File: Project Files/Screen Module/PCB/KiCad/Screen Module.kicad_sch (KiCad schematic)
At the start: 17 parts, among them J1 Conn_01x19_Male, J2 Conn_01x19_Male, J3 Conn_02x04_Top_Bottom, J4 Conn_02x03_Top_Bottom, Q1 BC817, SW1 SW_Push, SW2 SW_Push

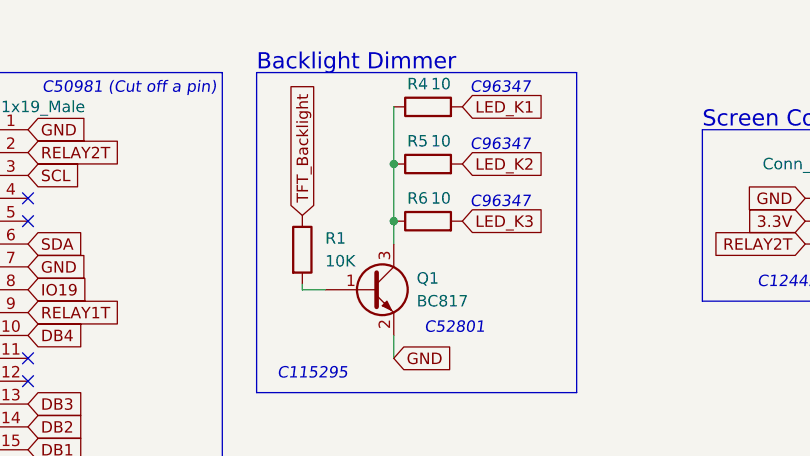
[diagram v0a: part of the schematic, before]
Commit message: Updated PCB to fix several issues Wall Module: Fixed relay flyback diodes pointing in the wrong direction.
Screen PCB:
Fixed display LED resistors to be a more suitable value.
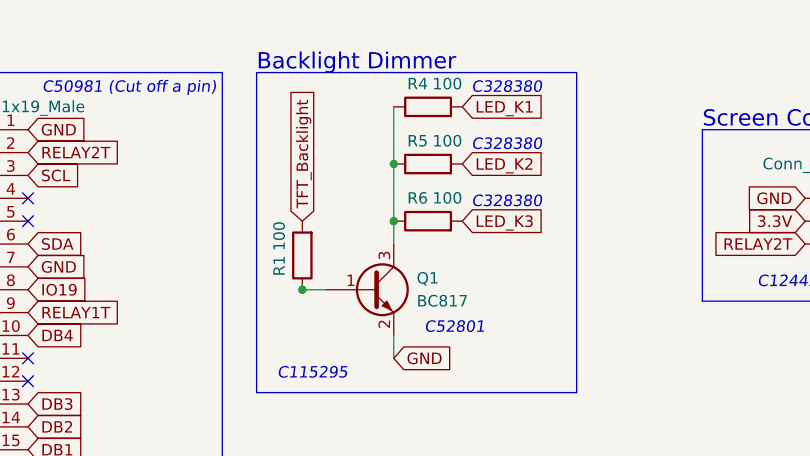
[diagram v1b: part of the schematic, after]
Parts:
- R1: value 10K -> 100
- R4, R5, R6: value 10 -> 100
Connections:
- net TFT_Backlight: now also R1.2; no longer R1.1
- net at Q1.1 (B): now also R1.1; no longer R1.2
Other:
- note added: "C328380"
- note removed: "C96347"
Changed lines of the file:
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@@
 (kicad_sch (version 20211123) (generator eeschema)
   (paper "A4")
+  (junction (at 87.63 45.72) (diameter 0) (color 0 0 0 0)
+  )
   (junction (at 97.79 38.1) (diameter 0) (color 0 0 0 0)
   )
@@
   )
   (text "3.3V\nEN\nVP\nVN\n34\n35\n32\n33\n25\n26\n27\n14\n12\nGND\n13\nD2\nD3\nCMD\n5V"
-    (at 41.91 74.93 0)
+    (at 41.91 74.93 180)
     (effects (font (size 1.55 1.55)) (justify right bottom))
   )
@@
     (effects (font (size 1.8 1.8)) (justify left bottom))
   )
-  (text "C96347" (at 113.03 30.48 180)
+  (text "C328380" (at 114.3 30.48 180)
     (effects (font (size 1.27 1.27) italic) (justify right bottom))
   )
   (text "GND\n23\n22\nTX\nRX\n21\nGND\n19\n18\n5\n17\n16\n4\n0\n2\n15\nD1\nD0\nCLK"
-    (at 52.07 74.93 0)
+    (at 52.07 74.93 180)
     (effects (font (size 1.55 1.55)) (justify right bottom))
   )
@@
     (effects (font (size 1.27 1.27) italic) (justify left bottom))
   )
-  (text "C96347" (at 113.03 36.83 180)
+  (text "C328380" (at 114.3 36.83 180)
     (effects (font (size 1.27 1.27) italic) (justify right bottom))
   )
@@
     (effects (font (size 1.27 1.27) italic) (justify right bottom))
   )
-  (text "C96347" (at 113.03 24.13 180)
+  (text "C328380" (at 114.3 24.13 180)
     (effects (font (size 1.27 1.27) italic) (justify right bottom))
   )
@@
     )
   )
-  (global_label "TFT_Backlight" (shape input) (at 87.63 37.465 90) (fields_autoplaced)
-    (effects (font (size 1.27 1.27)) (justify left))
-    (property "Intersheet References" "${INTERSHEET_REFS}" (id 0) (at 87.7094 22.2309 90)
+  (global_label "TFT_Backlight" (shape input) (at 87.63 38.1 90) (fields_autoplaced)
+    (effects (font (size 1.27 1.27)) (justify left))
+    (property "Intersheet References" "${INTERSHEET_REFS}" (id 0) (at 87.7094 22.8659 90)
       (effects (font (size 1.27 1.27)) (justify left) hide)
     )
@@
       (effects (font (size 1.27 1.27)) (justify left))
     )
-    (property "Value" "10" (id 1) (at 104.14 29.21 90)
+    (property "Value" "100" (id 1) (at 105.41 29.21 90)
       (effects (font (size 1.27 1.27)) (justify left))
     )
@@
       (effects (font (size 1.27 1.27)) (justify left))
     )
-    (property "Value" "10" (id 1) (at 104.14 35.56 90)
+    (property "Value" "100" (id 1) (at 105.41 35.56 90)
       (effects (font (size 1.27 1.27)) (justify left))
     )
@@
       (effects (font (size 1.27 1.27)) (justify left))
     )
-    (property "Value" "10" (id 1) (at 104.14 22.86 90)
+    (property "Value" "100" (id 1) (at 105.41 22.86 90)
       (effects (font (size 1.27 1.27)) (justify left))
     )
@@
     )
     (property "Datasheet" "~" (id 3) (at 101.6 25.4 0)
-      (effects (font (size 1.27 1.27)) hide)
-    )
-    (pin "1")
-    (pin "2")
-  )
-  (symbol (lib_id "Device:R") (at 87.63 41.275 0) (unit 1)
-    (in_bom yes) (on_board yes) (fields_autoplaced)
-    (property "Reference" "R1" (id 0) (at 90.17 40.0049 0)
-      (effects (font (size 1.27 1.27)) (justify left))
-    )
-    (property "Value" "10K" (id 1) (at 90.17 42.5449 0)
-      (effects (font (size 1.27 1.27)) (justify left))
-    )
-    (property "Footprint" "Resistor_SMD:R_0805_2012Metric" (id 2) (at 85.852 41.275 90)
-      (effects (font (size 1.27 1.27)) hide)
-    )
-    (property "Datasheet" "~" (id 3) (at 87.63 41.275 0)
       (effects (font (size 1.27 1.27)) hide)
     )
@@
     (pin "9")
   )
+  (symbol (lib_id "Device:R") (at 87.63 41.91 180) (unit 1)
+    (in_bom yes) (on_board yes)
+    (property "Reference" "R1" (id 0) (at 85.09 41.91 90)
+      (effects (font (size 1.27 1.27)) (justify left))
+    )
+    (property "Value" "100" (id 1) (at 85.09 38.1 90)
+      (effects (font (size 1.27 1.27)) (justify left))
+    )
+    (property "Footprint" "Resistor_SMD:R_0805_2012Metric" (id 2) (at 89.408 41.91 90)
+      (effects (font (size 1.27 1.27)) hide)
+    )
+    (property "Datasheet" "~" (id 3) (at 87.63 41.91 0)
+      (effects (font (size 1.27 1.27)) hide)
+    )
+    (pin "1")
+    (pin "2")
+  )
   (symbol (lib_id "Connector_Generic:Conn_01x06") (at 62.23 99.06 0) (unit 1)
     (in_bom yes) (on_board yes)
@@
       (reference "Q1") (unit 1) (value "BC817") (footprint "Package_TO_SOT_SMD:SOT-23")
     )
-    (path "/7898133f-3898-43f4-89ca-8b8f8a4a7a22"
-      (reference "R1") (unit 1) (value "10K") (footprint "Resistor_SMD:R_0805_2012Metric")
+    (path "/ec8978e6-ff0f-4a77-aecb-deea04e88bc9"
+      (reference "R1") (unit 1) (value "100") (footprint "Resistor_SMD:R_0805_2012Metric")
     )
     (path "/1c78a6d0-9f83-41ed-abd2-648ed65b4bd9"
@@
     )
     (path "/6d8b537a-8025-4318-8c36-54ee8cd71a2b"
-      (reference "R4") (unit 1) (value "10") (footprint "Resistor_SMD:R_0805_2012Metric")
+      (reference "R4") (unit 1) (value "100") (footprint "Resistor_SMD:R_0805_2012Metric")
     )
     (path "/1e981524-7543-43e6-b9d2-1cd61174482b"
-      (reference "R5") (unit 1) (value "10") (footprint "Resistor_SMD:R_0805_2012Metric")
+      (reference "R5") (unit 1) (value "100") (footprint "Resistor_SMD:R_0805_2012Metric")
     )
     (path "/59e14922-7e52-463f-8ed5-ba66b48f3e0a"
-      (reference "R6") (unit 1) (value "10") (footprint "Resistor_SMD:R_0805_2012Metric")
+      (reference "R6") (unit 1) (value "100") (footprint "Resistor_SMD:R_0805_2012Metric")
     )
     (path "/ce8963fb-9fc8-4f49-97e7-b45d61fb2e68"
